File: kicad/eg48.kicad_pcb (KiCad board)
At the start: 2 copper layers, 248.9 x 77.5 mm, 110 parts, among them SW1 PG1350, SW10 PG1350, SW11 PG1350, SW12 PG1350, SW13 PG1350, SW14 PG1350, SW15 PG1350, SW16 PG1350, SW17 PG1350, SW18 PG1350, SW19 PG1350, SW2 PG1350, SW20 PG1350, SW21 PG1350, SW22 PG1350, SW23 PG1350, SW24 PG1350, SW25 PG1350, SW26 PG1350, SW27 PG1350, SW28 PG1350, SW29 PG1350, SW3 PG1350, SW30 PG1350, SW31 PG1350, SW32 PG1350, SW33 PG1350, SW34 PG1350, SW35 PG1350, SW36 PG1350, SW37 PG1350, SW38 PG1350, SW39 PG1350, SW4 PG1350, SW40 PG1350, SW41 PG1350, SW42 PG1350, SW43 PG1350, SW44 PG1350, SW45 PG1350, SW46 PG1350, SW47 PG1350, SW48 PG1350, SW49 RotaryEncoder_Switch_MP, SW5 PG1350, SW6 PG1350, SW7 PG1350, SW8 PG1350, SW9 PG1350

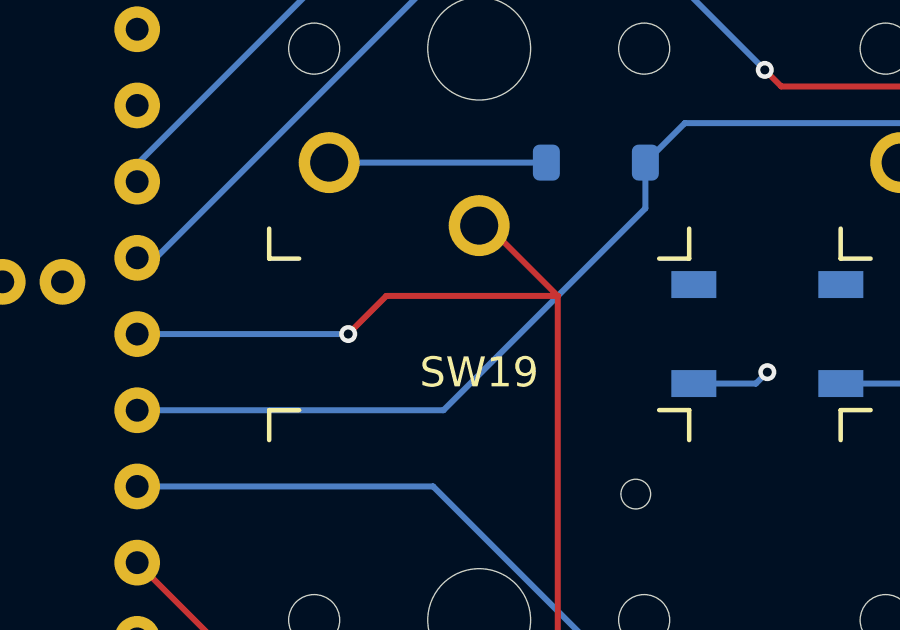
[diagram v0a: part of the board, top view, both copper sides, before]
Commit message: Update kicad files, add 3D models
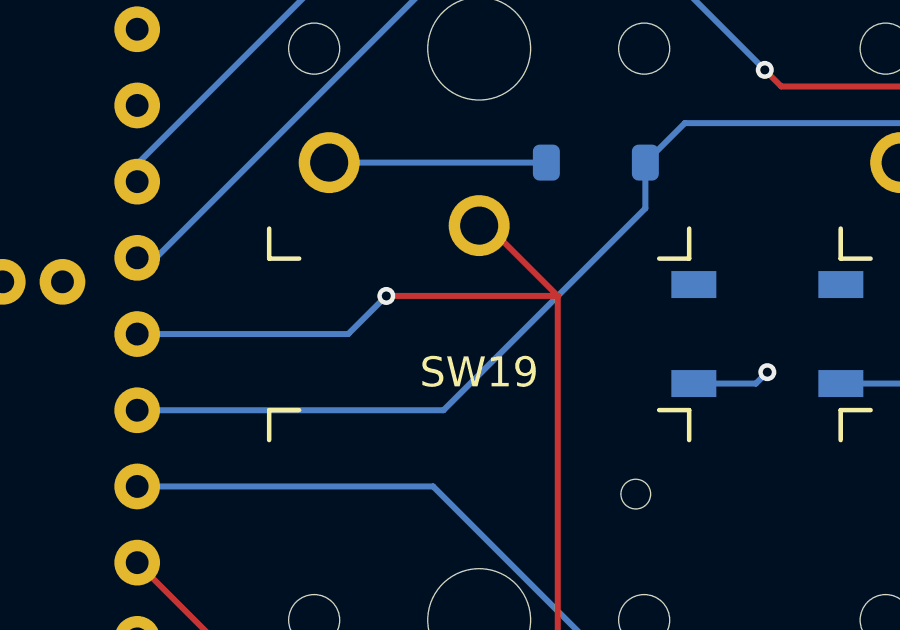
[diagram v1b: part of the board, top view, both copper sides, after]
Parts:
- SW49: value RotaryEncoder_Switch_MP -> EC11E12
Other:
- board text added: "EC11"
- board text added: "EC11E12- 15P30C"
- board text removed: "RE11"

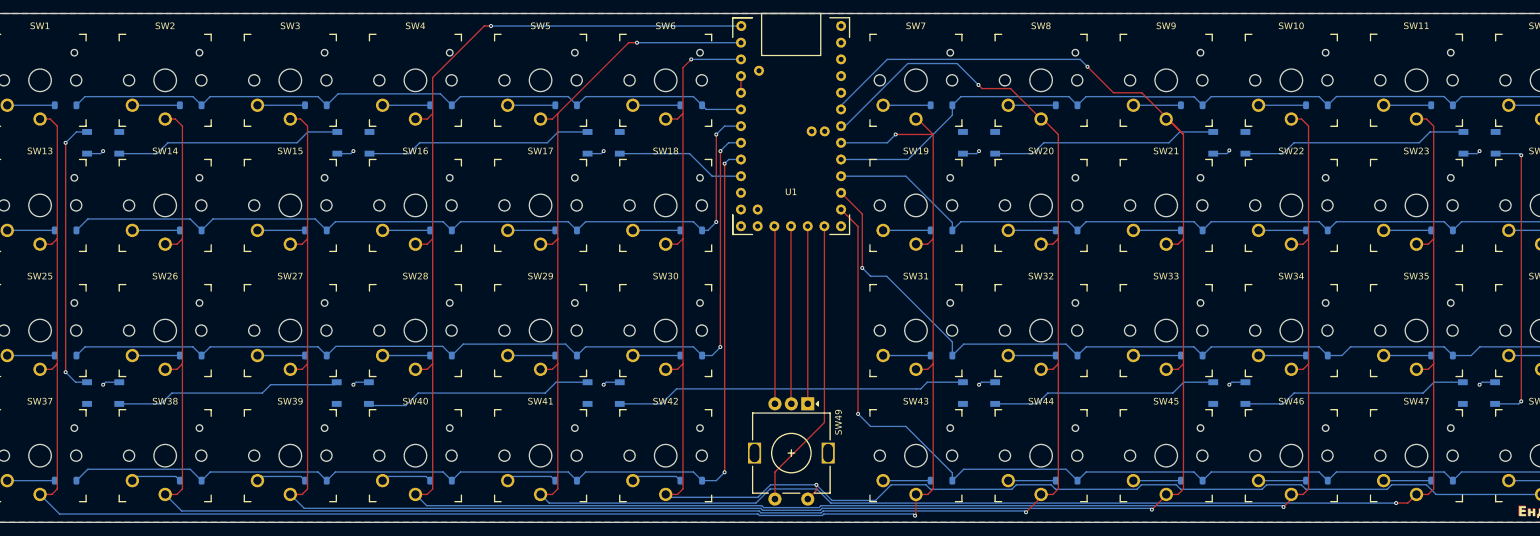
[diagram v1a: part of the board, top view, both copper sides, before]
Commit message: Kicad 9, nicer routing, clearance for rp2040
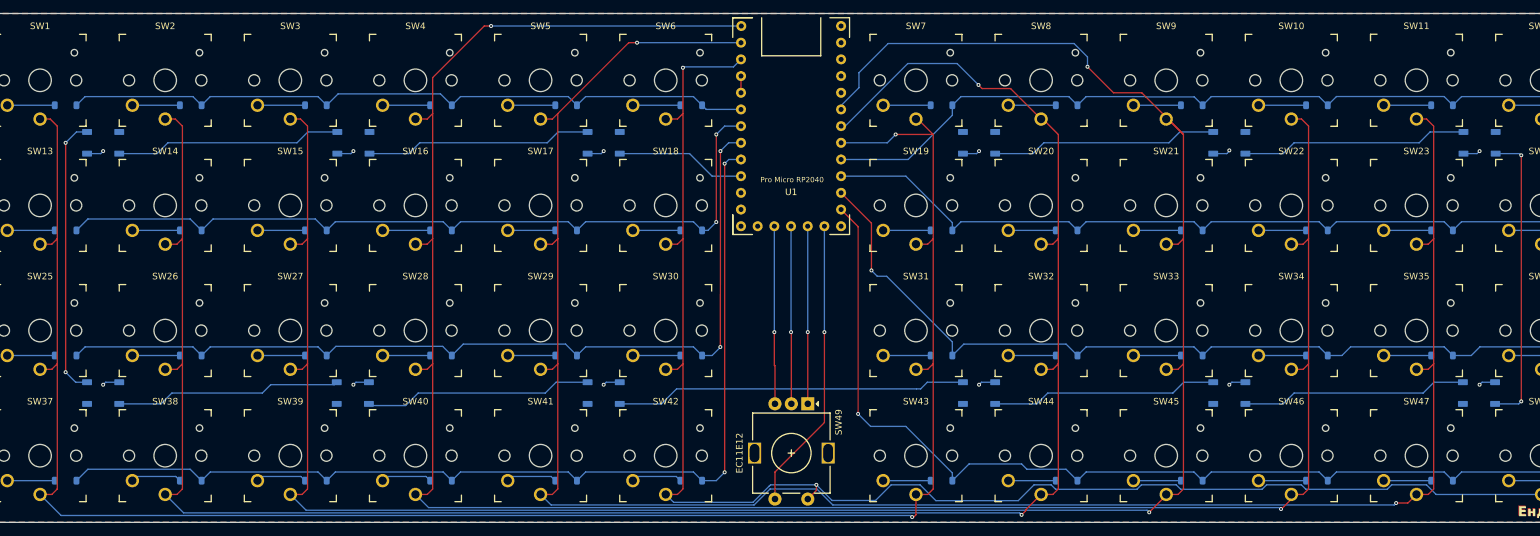
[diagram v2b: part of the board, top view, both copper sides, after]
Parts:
- U1: value ~ -> Pro Micro RP2040; footprint pro_micro_rp2040:pro_micro_rp2040 -> pro_micro_rp2040:pro_micro_rp2040_min
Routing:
- net /COL3: track 329.8 -> 334.1 mm
- net /COL6: track 294.4 -> 296.5 mm
- net /ROW8: track 152.5 -> 153.2 mm
- net /ROW6: track 134.3 -> 133.7 mm
- net Net-(U1-GP13): track 27.1 -> 27.2 mm, vias 0 -> 1
- net Net-(U1-GP14): vias 0 -> 1
- net Net-(U1-GP15): track 27.0 -> 27.1 mm, vias 0 -> 1
- net /ROW9: vias 0 -> 1
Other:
- board text added: "PBSM-40 STS-40P"
